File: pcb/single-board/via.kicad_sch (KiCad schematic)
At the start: 6 parts, among them J4 VIA, U18 74HC688, U19 W65C22NxP

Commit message: Further revising
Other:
- note added: "0x7F1X"
- note added: "Versatile Interface Adapter (VIA)"
- moved on the sheet: C23, C24, J4, R6, U18, U19

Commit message: Refactoring source
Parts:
- U18: value 74HC688 -> CD74HC688
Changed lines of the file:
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@@
 			)
 		)
-		(property "Value" "74HC688"
+		(property "Value" "CD74HC688"
 			(at 56.642 45.212 0)
 			(effects

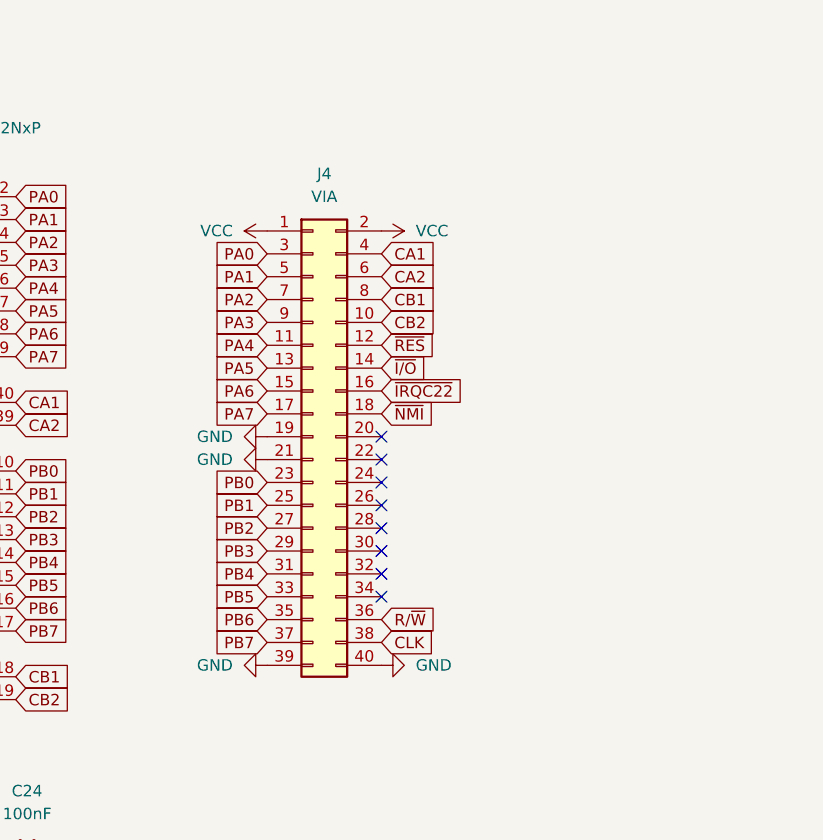
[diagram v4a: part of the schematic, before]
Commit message: Cleaning repository and completing SD-card reading using bitbang SPI
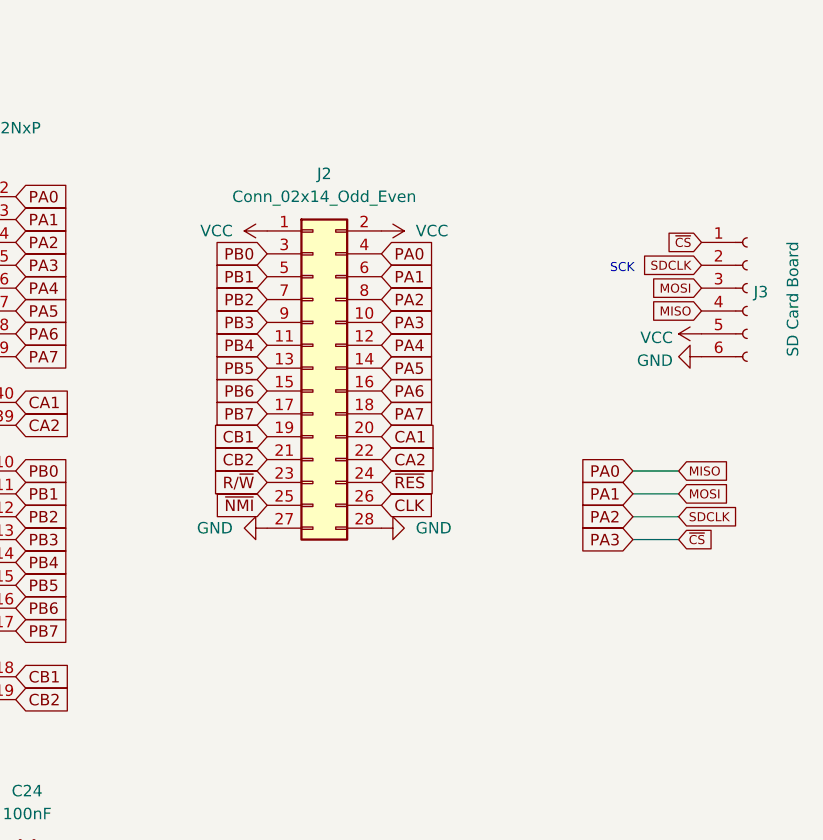
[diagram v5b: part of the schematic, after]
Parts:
- removed J4: VIA, Connector_PinHeader_2.54mm:PinHeader_2x20_P2.54mm_Vertical, symbol Connector_Generic:Conn_02x20_Odd_Even
- added J2: Conn_02x14_Odd_Even, Connector_PinHeader_2.54mm:PinHeader_2x14_P2.54mm_Vertical, symbol Connector_Generic:Conn_02x14_Odd_Even
- added J3: SD Card Board, sdcard-holder:sdcard-socket, symbol Connector:Conn_01x06_Female
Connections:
- net CA1: now also J2.20 (Pin_20)
- net CA2: now also J2.22 (Pin_22)
- net CB1: now also J2.19 (Pin_19)
- net CB2: now also J2.21 (Pin_21)
- net CLK: now also J2.26 (Pin_26)
- net GND: now also J2.27 (Pin_27), J2.28 (Pin_28), J3.6 (Pin_6)
- net PA2: now also J2.8 (Pin_8), J3.2 (Pin_2)
- net PA3: now also J2.10 (Pin_10), J3.1 (Pin_1)
- net PA4: now also J2.12 (Pin_12)
- net PA5: now also J2.14 (Pin_14)
- net PA6: now also J2.16 (Pin_16)
- net PA7: now also J2.18 (Pin_18)
- net PB0: now also J2.3 (Pin_3)
- net PB1: now also J2.5 (Pin_5)
- net PB2: now also J2.7 (Pin_7)
- net PB3: now also J2.9 (Pin_9)
- net PB4: now also J2.11 (Pin_11)
- net PB5: now also J2.13 (Pin_13)
- net PB6: now also J2.15 (Pin_15)
- net PB7: now also J2.17 (Pin_17)
- net R/~{W}: now also J2.23 (Pin_23)
- net VCC: now also J2.1 (Pin_1), J2.2 (Pin_2), J3.5 (Pin_5)
- net ~{NMI}: now also J2.25 (Pin_25)
- net ~{RES}: now also J2.24 (Pin_24)
- net PA0 renamed MISO
- net MISO: now also J2.4 (Pin_4), J3.4 (Pin_4)
- net PA1 renamed MOSI
- net MOSI: now also J2.6 (Pin_6), J3.3 (Pin_3)
- no-connect marks 8 -> 0
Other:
- note added: "SCK"
